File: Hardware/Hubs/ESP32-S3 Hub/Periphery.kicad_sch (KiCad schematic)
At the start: 10 parts, among them SW1 Mitsumi R-667996, SW2 Mitsumi R-667996, U2 IS31FL3726A-QFLS4, U3 THVD1420DRLR

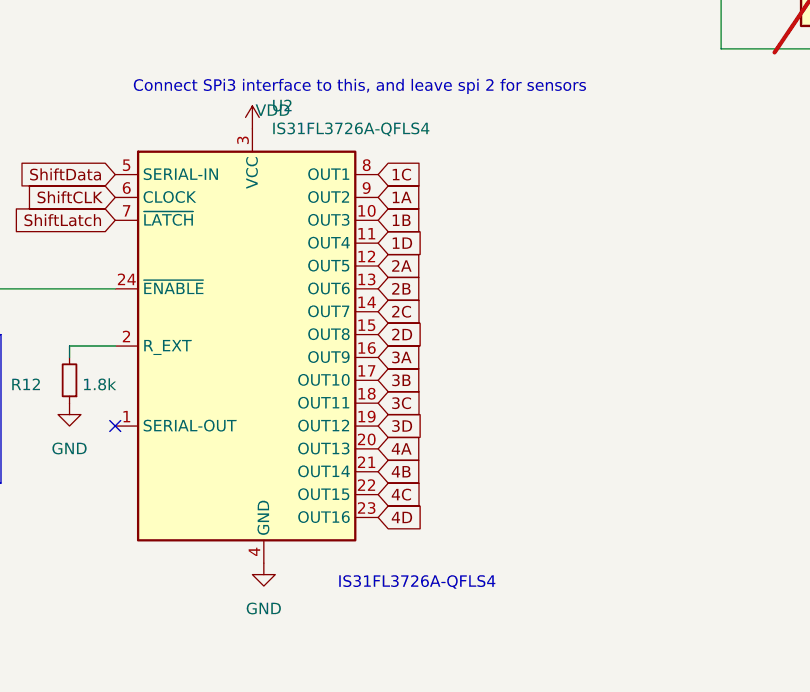
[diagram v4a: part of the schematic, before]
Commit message: Swapped around pins and routed main driver outputs
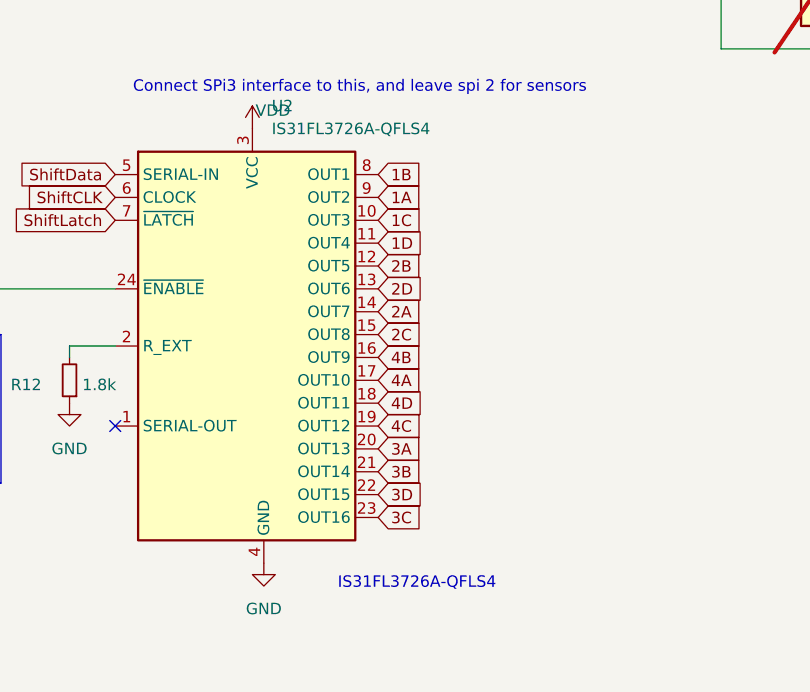
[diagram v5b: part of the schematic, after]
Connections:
- net 1B: now also U2.8 (OUT1); no longer U2.10 (OUT3)
- net 1C: now also U2.10 (OUT3); no longer U2.8 (OUT1)
- net 2A: now also U2.14 (OUT7); no longer U2.12 (OUT5)
- net 2B: now also U2.12 (OUT5); no longer U2.13 (OUT6)
- net 2C: now also U2.15 (OUT8); no longer U2.14 (OUT7)
- net 2D: now also U2.13 (OUT6); no longer U2.15 (OUT8)
- net 3A: now also U2.20 (OUT13); no longer U2.16 (OUT9)
- net 3B: now also U2.21 (OUT14); no longer U2.17 (OUT10)
- net 3C: now also U2.23 (OUT16); no longer U2.18 (OUT11)
- net 3D: now also U2.22 (OUT15); no longer U2.19 (OUT12)
- net 4A: now also U2.17 (OUT10); no longer U2.20 (OUT13)
- net 4B: now also U2.16 (OUT9); no longer U2.21 (OUT14)
- net 4C: now also U2.19 (OUT12); no longer U2.22 (OUT15)
- net 4D: now also U2.18 (OUT11); no longer U2.23 (OUT16)
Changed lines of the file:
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@@
 	(global_label "2D"
 		(shape input)
-		(at 90.17 133.35 0)
-		(fields_autoplaced yes)
-		(effects
-			(font
-				(size 1.27 1.27)
-			)
-			(justify left)
-		)
-		(property "Intersheetrefs" "${INTERSHEET_REFS}"
-			(at 95.6347 133.35 0)
+		(at 90.17 128.27 0)
+		(fields_autoplaced yes)
+		(effects
+			(font
+				(size 1.27 1.27)
+			)
+			(justify left)
+		)
+		(property "Intersheetrefs" "${INTERSHEET_REFS}"
+			(at 95.6347 128.27 0)
 			(effects
 				(font
@@
 	(global_label "4D"
 		(shape input)
+		(at 90.17 140.97 0)
+		(fields_autoplaced yes)
+		(effects
+			(font
+				(size 1.27 1.27)
+			)
+			(justify left)
+		)
+		(property "Intersheetrefs" "${INTERSHEET_REFS}"
+			(at 95.6347 140.97 0)
+			(effects
+				(font
+					(size 1.27 1.27)
+				)
+				(justify left)
+				(hide yes)
+			)
+		)
+	)
+	(global_label "4C"
+		(shape input)
+		(at 90.17 143.51 0)
+		(fields_autoplaced yes)
+		(effects
+			(font
+				(size 1.27 1.27)
+			)
+			(justify left)
+		)
+		(property "Intersheetrefs" "${INTERSHEET_REFS}"
+			(at 95.6347 143.51 0)
+			(effects
+				(font
+					(size 1.27 1.27)
+				)
+				(justify left)
+				(hide yes)
+			)
+		)
+	)
+	(global_label "1B"
+		(shape input)
+		(at 90.17 115.57 0)
+		(fields_autoplaced yes)
+		(effects
+			(font
+				(size 1.27 1.27)
+			)
+			(justify left)
+		)
+		(property "Intersheetrefs" "${INTERSHEET_REFS}"
+			(at 95.6347 115.57 0)
+			(effects
+				(font
+					(size 1.27 1.27)
+				)
+				(justify left)
+				(hide yes)
+			)
+		)
+	)
+	(global_label "3D"
+		(shape input)
+		(at 90.17 151.13 0)
+		(fields_autoplaced yes)
+		(effects
+			(font
+				(size 1.27 1.27)
+			)
+			(justify left)
+		)
+		(property "Intersheetrefs" "${INTERSHEET_REFS}"
+			(at 95.6347 151.13 0)
+			(effects
+				(font
+					(size 1.27 1.27)
+				)
+				(justify left)
+				(hide yes)
+			)
+		)
+	)
+	(global_label "2A"
+		(shape input)
+		(at 90.17 130.81 0)
+		(fields_autoplaced yes)
+		(effects
+			(font
+				(size 1.27 1.27)
+			)
+			(justify left)
+		)
+		(property "Intersheetrefs" "${INTERSHEET_REFS}"
+			(at 95.4533 130.81 0)
+			(effects
+				(font
+					(size 1.27 1.27)
+				)
+				(justify left)
+				(hide yes)
+			)
+		)
+	)
+	(global_label "3C"
+		(shape input)
 		(at 90.17 153.67 0)
 		(fields_autoplaced yes)
@@
 		)
 	)
-	(global_label "4C"
-		(shape input)
-		(at 90.17 151.13 0)
-		(fields_autoplaced yes)
-		(effects
-			(font
-				(size 1.27 1.27)
-			)
-			(justify left)
-		)
-		(property "Intersheetrefs" "${INTERSHEET_REFS}"
-			(at 95.6347 151.13 0)
-			(effects
-				(font
-					(size 1.27 1.27)
-				)
-				(justify left)
-				(hide yes)
-			)
-		)
-	)
-	(global_label "1B"
-		(shape input)
-		(at 90.17 120.65 0)
-		(fields_autoplaced yes)
-		(effects
-			(font
-				(size 1.27 1.27)
-			)
-			(justify left)
-		)
-		(property "Intersheetrefs" "${INTERSHEET_REFS}"
-			(at 95.6347 120.65 0)
-			(effects
-				(font
-					(size 1.27 1.27)
-				)
-				(justify left)
-				(hide yes)
-			)
-		)
-	)
-	(global_label "3D"
-		(shape input)
-		(at 90.17 143.51 0)
-		(fields_autoplaced yes)
-		(effects
-			(font
-				(size 1.27 1.27)
-			)
-			(justify left)
-		)
-		(property "Intersheetrefs" "${INTERSHEET_REFS}"
-			(at 95.6347 143.51 0)
-			(effects
-				(font
-					(size 1.27 1.27)
-				)
-				(justify left)
-				(hide yes)
-			)
-		)
-	)
-	(global_label "2A"
-		(shape input)
-		(at 90.17 125.73 0)
-		(fields_autoplaced yes)
-		(effects
-			(font
-				(size 1.27 1.27)
-			)
-			(justify left)
-		)
-		(property "Intersheetrefs" "${INTERSHEET_REFS}"
-			(at 95.4533 125.73 0)
-			(effects
-				(font
-					(size 1.27 1.27)
-				)
-				(justify left)
-				(hide yes)
-			)
-		)
-	)
-	(global_label "3C"
-		(shape input)
-		(at 90.17 140.97 0)
-		(fields_autoplaced yes)
-		(effects
-			(font
-				(size 1.27 1.27)
-			)
-			(justify left)
-		)
-		(property "Intersheetrefs" "${INTERSHEET_REFS}"
-			(at 95.6347 140.97 0)
-			(effects
-				(font
-					(size 1.27 1.27)
-				)
-				(justify left)
-				(hide yes)
-			)
-		)
-	)
 	(global_label "4B"
 		(shape input)
-		(at 90.17 148.59 0)
-		(fields_autoplaced yes)
-		(effects
-			(font
-				(size 1.27 1.27)
-			)
-			(justify left)
-		)
-		(property "Intersheetrefs" "${INTERSHEET_REFS}"
-			(at 95.6347 148.59 0)
+		(at 90.17 135.89 0)
+		(fields_autoplaced yes)
+		(effects
+			(font
+				(size 1.27 1.27)
+			)
+			(justify left)
+		)
+		(property "Intersheetrefs" "${INTERSHEET_REFS}"
+			(at 95.6347 135.89 0)
 			(effects
 				(font
@@
 	(global_label "2C"
 		(shape input)
-		(at 90.17 130.81 0)
-		(fields_autoplaced yes)
-		(effects
-			(font
-				(size 1.27 1.27)
-			)
-			(justify left)
-		)
-		(property "Intersheetrefs" "${INTERSHEET_REFS}"
-			(at 95.6347 130.81 0)
+		(at 90.17 133.35 0)
+		(fields_autoplaced yes)
+		(effects
+			(font
+				(size 1.27 1.27)
+			)
+			(justify left)
+		)
+		(property "Intersheetrefs" "${INTERSHEET_REFS}"
+			(at 95.6347 133.35 0)
 			(effects
 				(font
@@
 	(global_label "3A"
 		(shape input)
-		(at 90.17 135.89 0)
-		(fields_autoplaced yes)
-		(effects
-			(font
-				(size 1.27 1.27)
-			)
-			(justify left)
-		)
-		(property "Intersheetrefs" "${INTERSHEET_REFS}"
-			(at 95.4533 135.89 0)
+		(at 90.17 146.05 0)
+		(fields_autoplaced yes)
+		(effects
+			(font
+				(size 1.27 1.27)
+			)
+			(justify left)
+		)
+		(property "Intersheetrefs" "${INTERSHEET_REFS}"
+			(at 95.4533 146.05 0)
 			(effects
 				(font
@@
 	(global_label "2B"
 		(shape input)
-		(at 90.17 128.27 0)
-		(fields_autoplaced yes)
-		(effects
-			(font
-				(size 1.27 1.27)
-			)
-			(justify left)
-		)
-		(property "Intersheetrefs" "${INTERSHEET_REFS}"
-			(at 95.6347 128.27 0)
+		(at 90.17 125.73 0)
+		(fields_autoplaced yes)
+		(effects
+			(font
+				(size 1.27 1.27)
+			)
+			(justify left)
+		)
+		(property "Intersheetrefs" "${INTERSHEET_REFS}"
+			(at 95.6347 125.73 0)
 			(effects
 				(font
@@
 	(global_label "3B"
 		(shape input)
-		(at 90.17 138.43 0)
-		(fields_autoplaced yes)
-		(effects
-			(font
-				(size 1.27 1.27)
-			)
-			(justify left)
-		)
-		(property "Intersheetrefs" "${INTERSHEET_REFS}"
-			(at 95.6347 138.43 0)
+		(at 90.17 148.59 0)
+		(fields_autoplaced yes)
+		(effects
+			(font
+				(size 1.27 1.27)
+			)
+			(justify left)
+		)
+		(property "Intersheetrefs" "${INTERSHEET_REFS}"
+			(at 95.6347 148.59 0)
 			(effects
 				(font
@@
 	(global_label "4A"
 		(shape input)
-		(at 90.17 146.05 0)
-		(fields_autoplaced yes)
-		(effects
-			(font
-				(size 1.27 1.27)
-			)
-			(justify left)
-		)
-		(property "Intersheetrefs" "${INTERSHEET_REFS}"
-			(at 95.4533 146.05 0)
+		(at 90.17 138.43 0)
+		(fields_autoplaced yes)
+		(effects
+			(font
+				(size 1.27 1.27)
+			)
+			(justify left)
+		)
+		(property "Intersheetrefs" "${INTERSHEET_REFS}"
+			(at 95.4533 138.43 0)
 			(effects
 				(font
@@
 	(global_label "1C"
 		(shape input)
-		(at 90.17 115.57 0)
-		(fields_autoplaced yes)
-		(effects
-			(font
-				(size 1.27 1.27)
-			)
-			(justify left)
-		)
-		(property "Intersheetrefs" "${INTERSHEET_REFS}"
-			(at 95.6347 115.57 0)
-			(effects
-				(font
+		(at 90.17 120.65 0)
+		(fields_autoplaced yes)
+		(effects
+			(font
+				(size 1.27 1.27)
+			)
+			(justify left)
+		)
+		(property "Intersheetrefs" "${INTERSHEET_REFS}"
+			(at 95.6347 120.65 0)
+			(effects
+				(font
